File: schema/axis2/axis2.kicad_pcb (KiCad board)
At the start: 2 copper layers, 69 x 110 mm, 19 parts, among them J1 JA, J2 JB, J3 5VPower, J4 12VPower, J5 Power Motor 1, J6 Power Motor 2, J7 M1, J8 M2, J9 RC-PPM, Q1 BC547, U1 gy-9250, U2 L7805, U3 axis2-frame

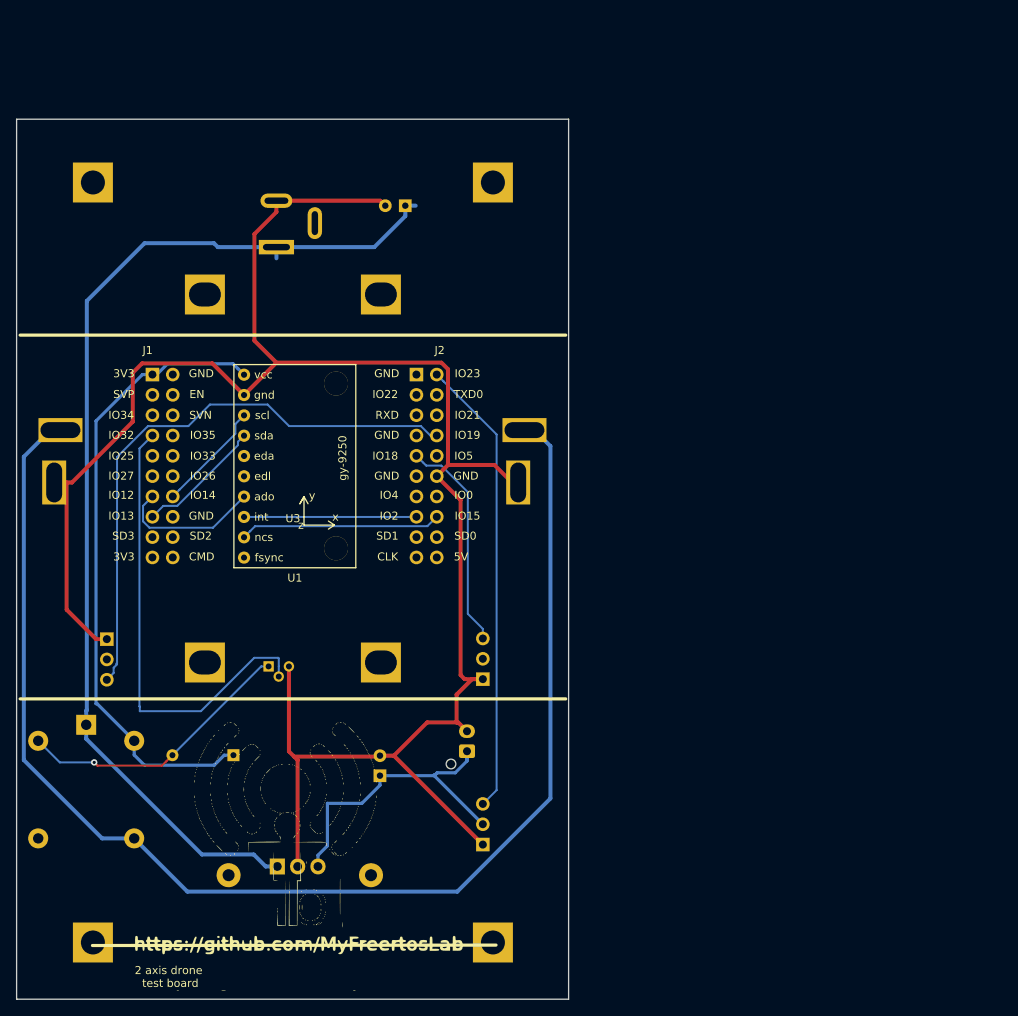
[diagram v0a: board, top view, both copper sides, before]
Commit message: Corretto scheda. Erano invertiti i pin degli headers
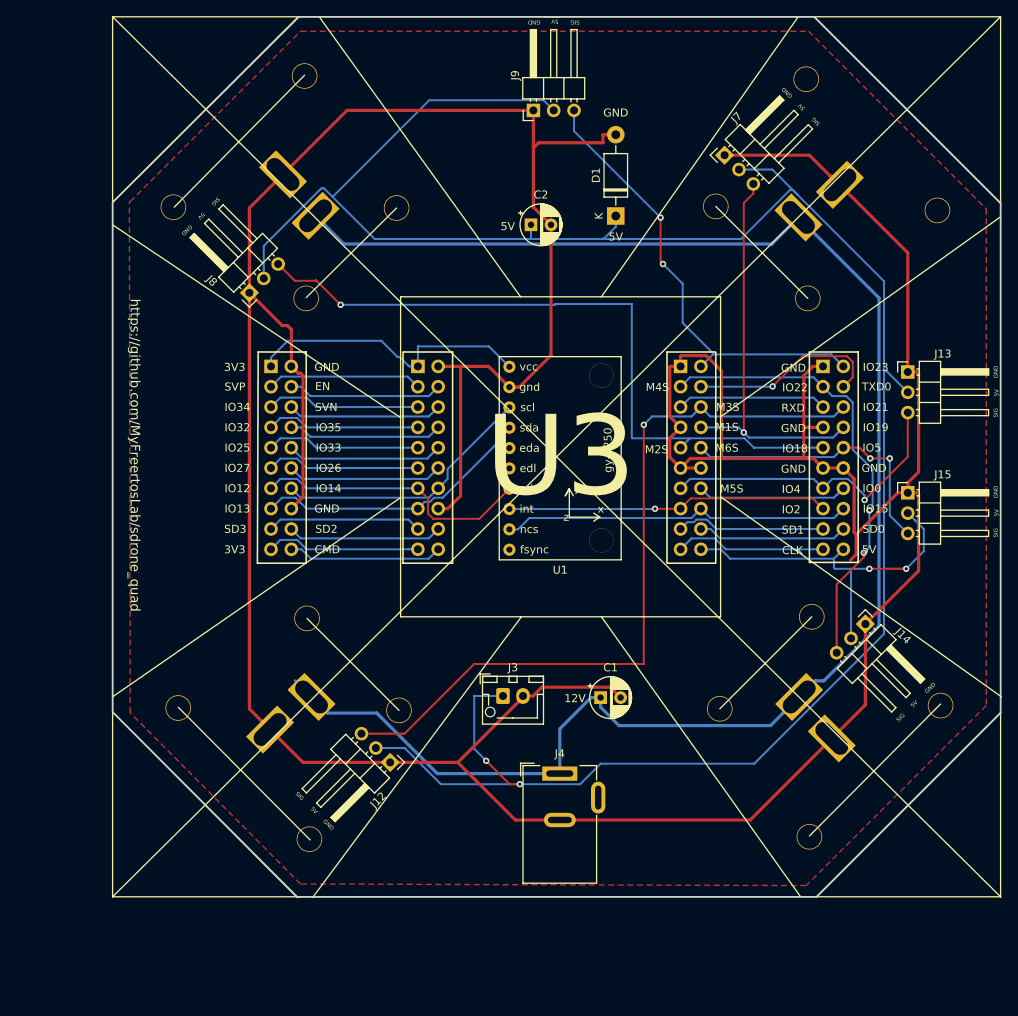
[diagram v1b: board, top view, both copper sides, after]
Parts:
- removed the G*** at (114.3, 142.1)
- removed HS1: Heatsink_Pad_2Pin, Heatsink:Heatsink_Stonecold_HS-132_32x14mm_2xFixation1.5mm
- removed Q1: BC547, Package_TO_SOT_THT:TO-92
- removed RLY1: G5LE-14_DC5, Relay_THT:Relay_SPDT_Omron-G5LE-1
- removed U2: L7805, Package_TO_SOT_THT:TO-220-3_Vertical
- added G***: LOGO, graphics:axis4-logo, B.Cu at (106.8, 91.3)
- added J10: Power Motor 3, Connector:Deans, B.Cu at (180.3, 126.0)
- added J11: Power Motor 4, Connector:Deans, B.Cu at (112.1, 125.7)
- added J12: M3, Connector_PinHeader_2.54mm:PinHeader_1x03_P2.54mm_Horizontal, F.Cu at (125.7, 130.4)
- added J13: M5, Connector_PinHeader_2.54mm:PinHeader_1x03_P2.54mm_Horizontal, F.Cu at (190.4, 81.6)
- added J14: M4, Connector_PinHeader_2.54mm:PinHeader_1x03_P2.54mm_Horizontal, F.Cu at (185.1, 113.1)
- added J15: M6, Connector_PinHeader_2.54mm:PinHeader_1x03_P2.54mm_Horizontal, F.Cu at (190.4, 96.7)
- added J16: JA1, Connector_PinSocket_2.54mm:PinSocket_2x10_P2.54mm_Vertical, B.Cu at (110.8, 80.9)
- added J17: JB1, Connector_PinSocket_2.54mm:PinSocket_2x10_P2.54mm_Vertical, B.Cu at (179.8, 80.9)
- C1, C2, J3, J4, J7, J8, J9: moved to F.Cu
- D1: value D_ALT -> 1N4007; footprint Diode_THT:D_DO-34_SOD68_P7.62mm_Horizontal -> Diode_THT:D_DO-41_SOD81_P10.16mm_Horizontal; moved to F.Cu
- U3: value axis2-frame -> axis4-symbol; footprint axis2:axis2-footprint -> axis4:axis4-frame
- moved J5 102.5 mm to (180.5, 58.8), turned to 315 degrees
- moved J7 98.1 mm to (167.5, 54.5), turned to 45 degrees
- moved J9 92.0 mm to (143.6, 48.9), turned to 90 degrees
- moved D1 82.6 mm to (153.9, 62.1), turned to 90 degrees
- moved J4 74.7 mm to (146.9, 131.8)
- moved C2 71.4 mm to (143.3, 63.2), turned to 0 degrees
- moved C1 66.2 mm to (152.0, 122.3), turned to 0 degrees
- moved J8 56.4 mm to (108.1, 71.7), turned to 135 degrees
- moved J6 46.2 mm to (112.9, 58.3), turned to 45 degrees
- moved U3 34.7 mm to (146.5, 92.2)
- moved J1 33.2 mm to (129.2, 80.9)
- moved U1 33.2 mm to (153.3, 93.7)
- moved J2 33.0 mm to (162.0, 80.9)
- moved J3 8.24 mm to (139.8, 122.1), turned to 0 degrees
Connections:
- D1 pad 1: +3V3 -> +5V
- D1 pad 2: Net-(D1-Pad2) -> GND
- J1 pad 16: Net-(J1-Pad16) -> GND
- J1 pad 2: Net-(J1-Pad2) -> GND
- J1 pad 7: GPIO32 -> Net-(J1-Pad7)
- J2 pad 1: Net-(J2-Pad1) -> GND
- J2 pad 10: Net-(J2-Pad10) -> M6S
- J2 pad 11: Net-(J2-Pad11) -> GND
- J2 pad 13: Net-(J2-Pad13) -> M5S
- J2 pad 20: Net-(J2-Pad20) -> +5V
- J2 pad 3: Net-(J2-Pad3) -> M4S
- J2 pad 6: Net-(J2-Pad6) -> M3S
- J2 pad 7: Net-(J2-Pad7) -> GND
- J5 pad 1: +12VM -> +12V
- J6 pad 1: +12VM -> +12V
- J7 pad 2: Net-(J7-Pad2) -> +5V
- J8 pad 2: Net-(J8-Pad2) -> +5V
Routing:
- net +5V: track 38.7 -> 330.0 mm, vias 0 -> 4
- net GND: track 247.9 -> 513.5 mm
- net +12VM: track 171.2 -> 0.00 mm
- net M3S: track 0.00 -> 95.6 mm, vias 0 -> 1
- net +12V: track 133.9 -> 210.7 mm
- net M2S: track 27.4 -> 90.1 mm, vias 0 -> 1
- net GPIO32: track 57.6 -> 0.00 mm
- net M4S: track 0.00 -> 57.5 mm, vias 0 -> 2
- net +3V3: track 79.3 -> 36.8 mm
- net M5S: track 0.00 -> 39.0 mm, vias 0 -> 1
- net M6S: track 0.00 -> 35.5 mm, vias 0 -> 2
- net Net-(D1-Pad2): track 35.2 -> 0.00 mm, vias 1 -> 0
- net Net-(J17-Pad4): track 0.00 -> 24.4 mm, vias 0 -> 1
- net M1S: track 73.0 -> 50.4 mm, vias 0 -> 1
- net Net-(J1-Pad12): track 0.00 -> 19.5 mm
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- added copper zone on F.Cu, net GND
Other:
- board size 69 x 110 mm -> 111 x 110 mm
- net class 12V added: clearance 0.3, trace_width 0.4, via_dia 0.7, via_drill 0.5
- net class Power12V removed
- net class Power5V removed
- rule pad_to_mask_clearance: 0.051 -> 0
- board text added: "12V"
- board text added: "M1S"
- board text added: "M2S"
- board text added: "M3S"
- board text added: "M4S"
- board text added: "M5S"
- board text added: "M6S"
- board text added: "SIG"
- board text added: "by Andrea Lambruschini"
- board text added: "https://github.com/MyFreertosLab/sdrone_quad"
- board text removed: "+"
- board text removed: "+12V"
- board text removed: "+5V"
- board text removed: "-"
- board text removed: "2 axis drone test board"
- board text removed: "INT"
- board text removed: "J1"
- board text removed: "J2"
- board text removed: "MISO"
- board text removed: "MOSI"
- board text removed: "NCS"
- board text removed: "SCL"
- board text removed: "Signal"
- board text removed: "https://github.com/MyFreertosLab"

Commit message: Tolto alimentazione 12V dalla scheda. Utilizzo alimentazione separata per i motori
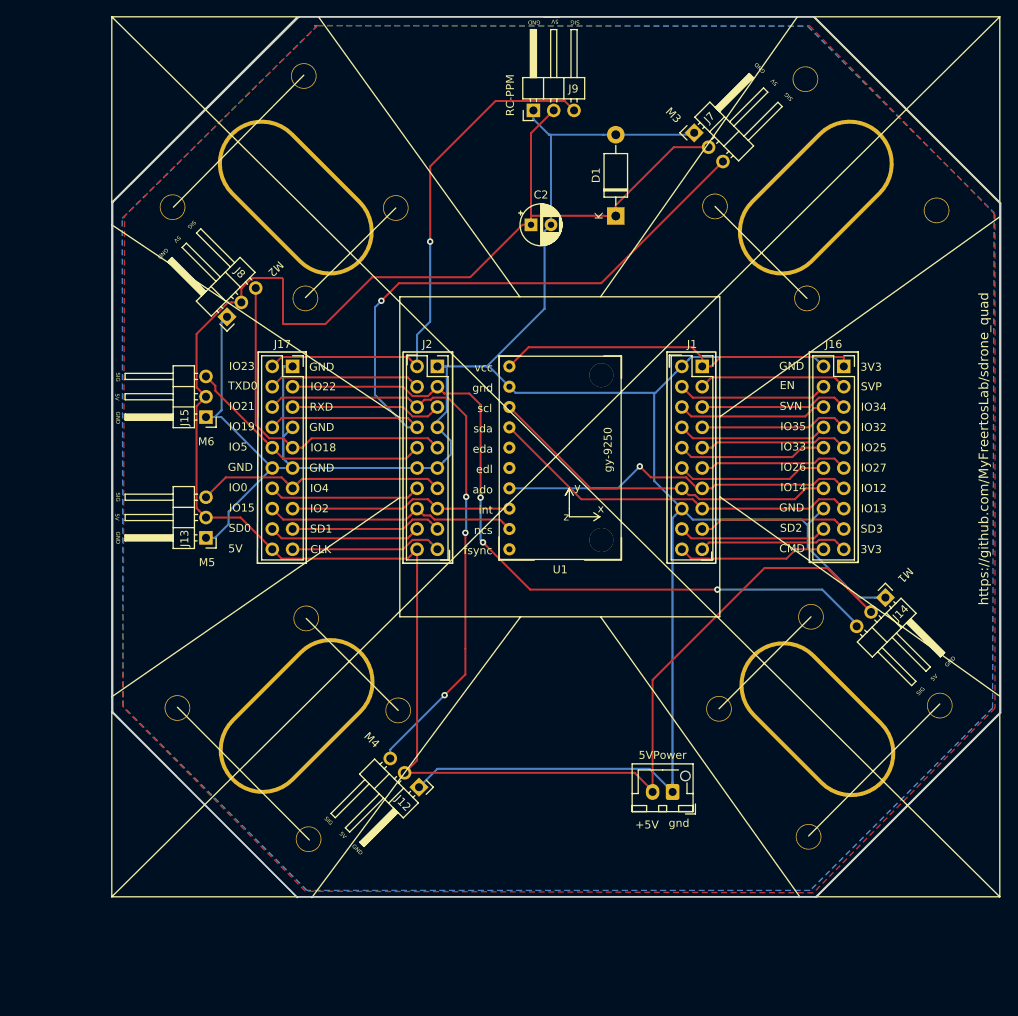
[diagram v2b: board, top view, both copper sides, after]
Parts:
- removed C1: 100uF, Capacitor_THT:CP_Radial_D5.0mm_P2.50mm
- removed G***: LOGO, graphics:axis4-logo
- removed J10: Power Motor 3, Connector:Deans
- removed J11: Power Motor 4, Connector:Deans
- removed J4: 12VPower, Connector_BarrelJack:BarrelJack_Wuerth_6941xx301002
- removed J5: Power Motor 1, Connector:Deans
- removed J6: Power Motor 2, Connector:Deans
- J1, J16, J17, J2: moved to F.Cu
- J12: value M3 -> M4
- J14: value M4 -> M1
- J7: value M1 -> M3
- moved J13 90.1 mm to (102.7, 102.3), turned to 180 degrees
- moved J15 88.2 mm to (102.7, 87.2), turned to 180 degrees
- moved J16 71.6 mm to (182.4, 80.9), turned to 0 degrees
- moved J17 66.3 mm to (113.5, 80.9), turned to 0 degrees
- moved J1 35.5 mm to (164.7, 80.9), turned to 0 degrees
- moved J2 30.4 mm to (131.6, 80.9), turned to 0 degrees
- moved J3 24.4 mm to (161.0, 134.1), turned to 180 degrees
- moved J12 4.75 mm to (129.3, 133.5)
- moved J7 4.72 mm to (163.7, 51.7)
- moved J14 4.14 mm to (187.6, 109.8)
- moved J8 4.10 mm to (105.3, 74.7)
- moved U3 0.10 mm to (146.4, 92.2)
- moved U1 0.05 mm to (153.3, 93.6)
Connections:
- C2 pad 2: GND -> /GND
- D1 pad 2: GND -> /GND
- J1 pad 16: GND -> /GND
- J1 pad 2: GND -> /GND
- J12 pad 1: GND -> /GND
- J12 pad 3: M3S -> M4S
- J13 pad 1: GND -> /GND
- J14 pad 1: GND -> /GND
- J14 pad 3: M4S -> M1S
- J15 pad 1: GND -> /GND
- J16 pad 16: GND -> /GND
- J16 pad 2: GND -> /GND
- J17 pad 1: GND -> /GND
- J17 pad 11: GND -> /GND
- J17 pad 12: GND -> /GND
- J17 pad 3: M4S -> M1S
- J17 pad 6: M3S -> M4S
- J17 pad 7: GND -> /GND
- J17 pad 8: M1S -> M3S
- J2 pad 1: GND -> /GND
- J2 pad 11: GND -> /GND
- J2 pad 12: GND -> /GND
- J2 pad 3: M4S -> M1S
- J2 pad 6: M3S -> M4S
- J2 pad 7: GND -> /GND
- J2 pad 8: M1S -> M3S
- J3 pad 1: +5V -> /GND
- J3 pad 2: GND -> +5V
- J7 pad 1: GND -> /GND
- J7 pad 3: M1S -> M3S
- J8 pad 1: GND -> /GND
- J9 pad 1: GND -> /GND
- U1 pad 10: Net-(U1-Pad10) -> (no net)
- U1 pad 2: GND -> /GND
- U1 pad 5: Net-(U1-Pad5) -> (no net)
- U1 pad 6: Net-(U1-Pad6) -> (no net)
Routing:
- net GND: track 513.5 -> 0.00 mm
- net /GND: track 0.00 -> 319.7 mm
- net +12V: track 210.7 -> 0.00 mm
- net +5V: track 330.0 -> 263.1 mm, vias 4 -> 0
- net M2S: track 90.1 -> 42.0 mm, vias 1 -> 0
- net M1S: track 50.4 -> 93.9 mm, vias 1 -> 3
- net M4S: track 57.5 -> 73.4 mm, vias 2 -> 3
- net INT: track 40.3 -> 28.1 mm, vias 1 -> 0
- net NCS: track 43.8 -> 31.8 mm
- net MOSI: track 35.4 -> 47.0 mm
- net SCL: track 33.1 -> 44.6 mm
- net MISO: track 35.1 -> 45.0 mm, vias 0 -> 1
- net RCS: track 56.7 -> 66.6 mm, vias 2 -> 1
- net +3V3: track 36.8 -> 46.1 mm
- net M3S: track 95.6 -> 88.0 mm
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- added copper zone on F.Cu, net +5V
- added copper zone on B.Cu, net /GND
- removed copper zone on F.Cu, net GND
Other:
- net class 12V: trace_width 0.4 -> 0.8
- board text added: "+5V"
- board text added: "gnd"
- board text removed: "12V"
- board text removed: "M1S"
- board text removed: "M2S"
- board text removed: "M3S"
- board text removed: "M4S"
- board text removed: "M5S"
- board text removed: "M6S"
